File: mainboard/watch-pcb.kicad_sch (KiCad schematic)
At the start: 0 parts

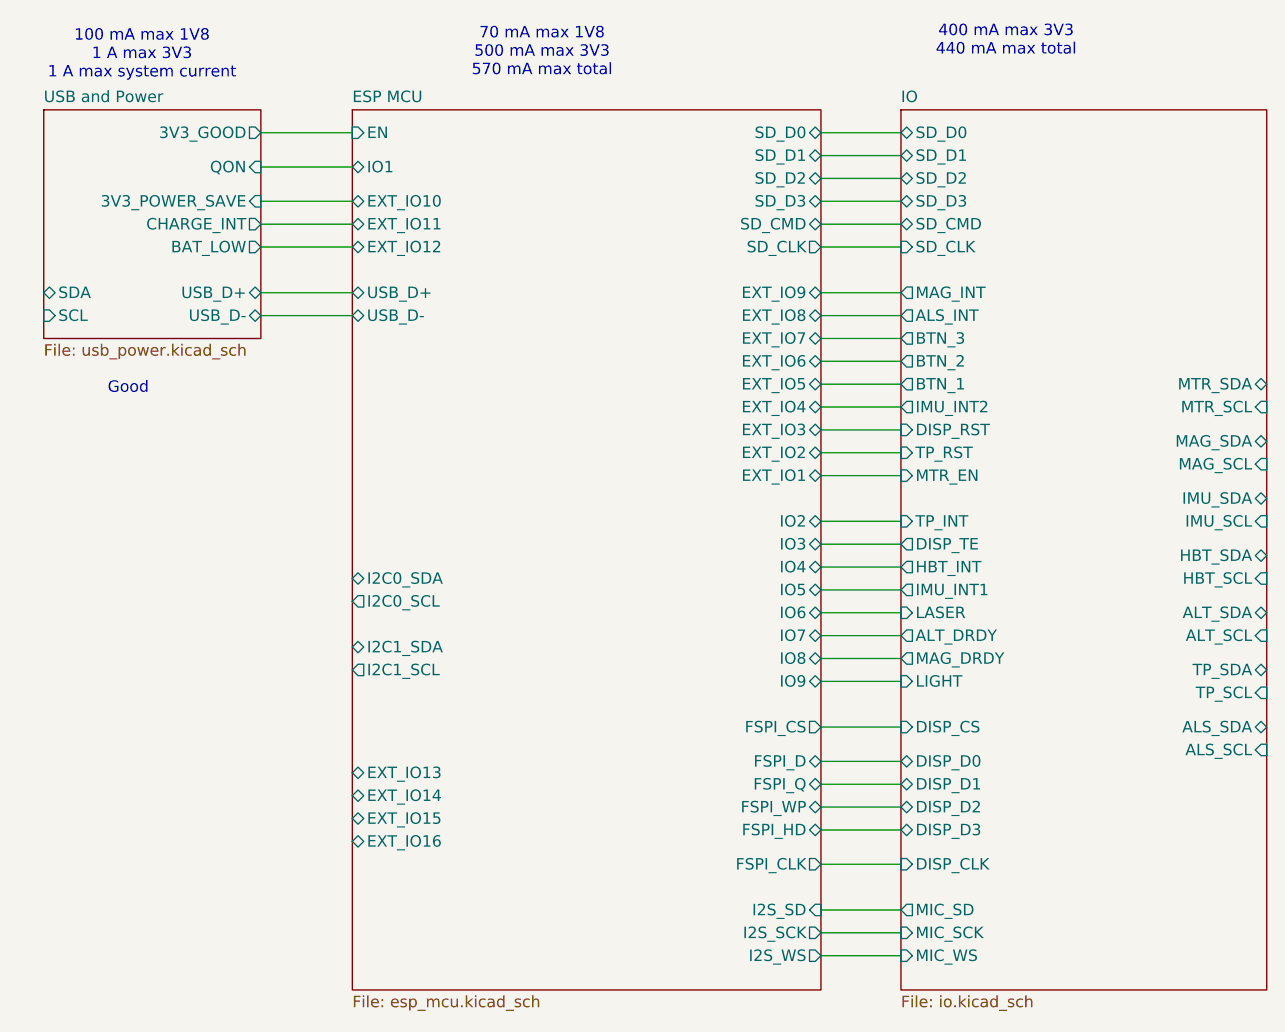
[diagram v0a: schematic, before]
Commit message: remove all features idrc abt from schematic
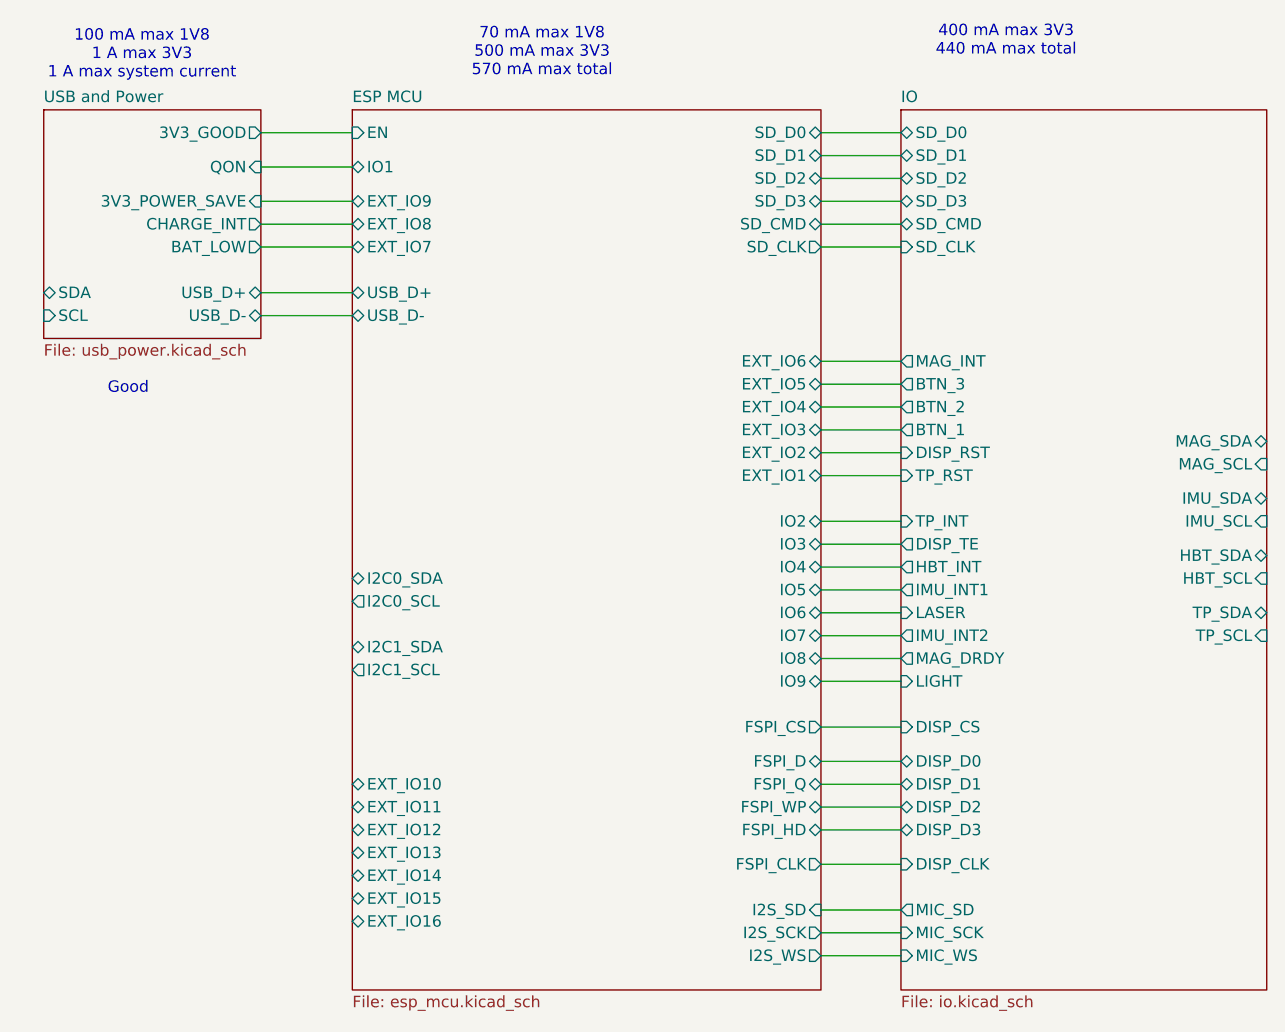
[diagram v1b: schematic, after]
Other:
- sheet IO ports: added none; removed ALS_INT, ALS_SCL, ALS_SDA, ALT_DRDY, ALT_SCL, ALT_SDA, MTR_EN, MTR_SCL, MTR_SDA
